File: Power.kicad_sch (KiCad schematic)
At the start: 37 parts, among them J10 Conn_01x01, U4 LMR51625YDDCR, U5 TLV74033PDBVR

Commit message: LCD connector, backlight, other work
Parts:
- removed D10, D12: LED, LED_SMD:LED_0603_1608Metric_Pad1.05x0.95mm_HandSolder, symbol Device:LED
- removed R22: 2.2k, Resistor_SMD:R_0603_1608Metric_Pad0.98x0.95mm_HandSolder, symbol Device:R
- removed R24: 120, Resistor_SMD:R_0603_1608Metric_Pad0.98x0.95mm_HandSolder, symbol Device:R
- D3, D4, D6: footprint Diode_SMD:D_SMA -> Diode_SMD:D_SOD-123F
- L2: value SRU1063A-4R7Y -> 6.8u; footprint Inductor_SMD:L_Bourns-SRU1028_10.0x10.0mm -> Inductor_SMD:L_Bourns-SRN4018

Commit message: fix swd connector orientation, modify 12v input
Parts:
- removed F1: Fuse, Fuse:Fuseholder_Blade_Mini_Keystone_3568, symbol Device:Fuse
- removed J10: Conn_01x01, Connector_PinHeader_2.54mm:PinHeader_1x01_P2.54mm_Vertical, symbol Connector_Generic:Conn_01x01
- removed JP1: SolderJumper_2_Open, Jumper:SolderJumper-2_P1.3mm_Open_RoundedPad1.0x1.5mm, symbol Jumper:SolderJumper_2_Open
- added F1: Polyfuse, Fuse:Fuse_1812_4532Metric_Pad1.30x3.40mm_HandSolder, symbol Device:Polyfuse
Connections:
- net +12V: now also D13.2 (A), F1.2
- net +12V_IN: now also F1.1
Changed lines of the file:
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@@
 	)
 	(junction
-		(at 43.18 82.55)
-		(diameter 0)
-		(color 0 0 0 0)
-	)
-	(junction
 		(at 96.52 110.49)
 		(diameter 0)
@@
 	(wire
 		(pts
-			(xy 35.56 82.55) (xy 43.18 82.55)
-		)
-		(stroke
-			(width 0)
-			(type default)
-		)
-	)
-	(wire
-		(pts
 			(xy 53.34 162.56) (xy 53.34 157.48)
 		)
@@
 	(wire
 		(pts
-			(xy 43.18 82.55) (xy 48.26 82.55)
-		)
-		(stroke
-			(width 0)
-			(type default)
-		)
-	)
-	(wire
-		(pts
 			(xy 73.66 90.17) (xy 80.01 90.17)
 		)
@@
 	(wire
 		(pts
-			(xy 38.1 92.71) (xy 43.18 92.71)
-		)
-		(stroke
-			(width 0)
-			(type default)
-		)
-	)
-	(wire
-		(pts
 			(xy 124.46 80.01) (xy 132.08 80.01)
 		)
@@
 	(wire
 		(pts
-			(xy 43.18 92.71) (xy 43.18 82.55)
-		)
-		(stroke
-			(width 0)
-			(type default)
-		)
-	)
-	(wire
-		(pts
 			(xy 58.42 123.19) (xy 58.42 110.49)
 		)
@@
 	(wire
 		(pts
-			(xy 27.94 82.55) (xy 24.13 82.55)
+			(xy 24.13 82.55) (xy 48.26 82.55)
 		)
 		(stroke
@@
 	)
 	(symbol
-		(lib_id "Jumper:SolderJumper_2_Open")
-		(at 31.75 82.55 0)
-		(unit 1)
-		(exclude_from_sim no)
-		(in_bom no)
-		(on_board yes)
-		(dnp no)
-		(fields_autoplaced yes)
-		(property "Reference" "JP1"
-			(at 31.75 76.2 0)
-			(effects
-				(font
-					(size 1.27 1.27)
-				)
-			)
-		)
-		(property "Value" "SolderJumper_2_Open"
-			(at 31.75 78.74 0)
-			(effects
-				(font
-					(size 1.27 1.27)
-				)
-			)
-		)
-		(property "Footprint" "Jumper:SolderJumper-2_P1.3mm_Open_RoundedPad1.0x1.5mm"
-			(at 31.75 82.55 0)
-			(effects
-				(font
-					(size 1.27 1.27)
-				)
-				(hide yes)
-			)
-		)
-		(property "Datasheet" "~"
-			(at 31.75 82.55 0)
-			(effects
-				(font
-					(size 1.27 1.27)
-				)
-				(hide yes)
-			)
-		)
-		(property "Description" "Solder Jumper, 2-pole, open"
-			(at 31.75 82.55 0)
-			(effects
-				(font
-					(size 1.27 1.27)
-				)
-				(hide yes)
-			)
-		)
-		(pin "2"
-		)
-		(pin "1"
-		)
-		(instances
-			(project ""
-				(path "/f2bb7816-6b2a-47fd-8906-eb4aedd6f9e6/5e700bbe-1f69-4433-b621-e458f2a62014"
-					(reference "JP1")
-					(unit 1)
-				)
-			)
-		)
-	)
-	(symbol
 		(lib_id "Device:R")
 		(at 63.5 38.1 0)
@@
 	)
 	(symbol
+		(lib_id "Device:Polyfuse")
+		(at 50.8 33.02 90)
+		(unit 1)
+		(exclude_from_sim no)
+		(in_bom yes)
+		(on_board yes)
+		(dnp no)
+		(fields_autoplaced yes)
+		(property "Reference" "F1"
+			(at 50.8 26.67 90)
+			(effects
+				(font
+					(size 1.27 1.27)
+				)
+			)
+		)
+		(property "Value" "Polyfuse"
+			(at 50.8 29.21 90)
+			(effects
+				(font
+					(size 1.27 1.27)
+				)
+			)
+		)
+		(property "Footprint" "Fuse:Fuse_1812_4532Metric_Pad1.30x3.40mm_HandSolder"
+			(at 55.88 31.75 0)
+			(effects
+				(font
+					(size 1.27 1.27)
+				)
+				(justify left)
+				(hide yes)
+			)
+		)
+		(property "Datasheet" "~"
+			(at 50.8 33.02 0)
+			(effects
+				(font
+					(size 1.27 1.27)
+				)
+				(hide yes)
+			)
+		)
+		(property "Description" "Resettable fuse, polymeric positive temperature coefficient"
+			(at 50.8 33.02 0)
+			(effects
+				(font
+					(size 1.27 1.27)
+				)
+				(hide yes)
+			)
+		)
+		(pin "2"
+		)
+		(pin "1"
+		)
+		(instances
+			(project "LV3-Dash"
+				(path "/f2bb7816-6b2a-47fd-8906-eb4aedd6f9e6/5e700bbe-1f69-4433-b621-e458f2a62014"
+					(reference "F1")
+					(unit 1)
+				)
+			)
+		)
+	)
+	(symbol
 		(lib_id "Device:C")
 		(at 43.18 161.29 0)
@@
 	)
 	(symbol
-		(lib_id "Device:Fuse")
-		(at 50.8 33.02 90)
-		(unit 1)
-		(exclude_from_sim no)
-		(in_bom yes)
-		(on_board yes)
-		(dnp no)
-		(fields_autoplaced yes)
-		(property "Reference" "F1"
-			(at 50.8 26.67 90)
-			(effects
-				(font
-					(size 1.27 1.27)
-				)
-			)
-		)
-		(property "Value" "Fuse"
-			(at 50.8 29.21 90)
-			(effects
-				(font
-					(size 1.27 1.27)
-				)
-			)
-		)
-		(property "Footprint" "Fuse:Fuseholder_Blade_Mini_Keystone_3568"
-			(at 50.8 34.798 90)
-			(effects
-				(font
-					(size 1.27 1.27)
-				)
-				(hide yes)
-			)
-		)
-		(property "Datasheet" "~"
-			(at 50.8 33.02 0)
-			(effects
-				(font
-					(size 1.27 1.27)
-				)
-				(hide yes)
-			)
-		)
-		(property "Description" "Fuse"
-			(at 50.8 33.02 0)
-			(effects
-				(font
-					(size 1.27 1.27)
-				)
-				(hide yes)
-			)
-		)
-		(pin "2"
-		)
-		(pin "1"
-		)
-		(instances
-			(project ""
-				(path "/f2bb7816-6b2a-47fd-8906-eb4aedd6f9e6/5e700bbe-1f69-4433-b621-e458f2a62014"
-					(reference "F1")
-					(unit 1)
-				)
-			)
-		)
-	)
-	(symbol
 		(lib_id "Device:C")
 		(at 76.2 46.99 0)
@@
 					(unit 1)
 				)
-			)
-		)
-	)
-	(symbol
-		(lib_id "Connector_Generic:Conn_01x01")
-		(at 33.02 92.71 180)
-		(unit 1)
-		(exclude_from_sim no)
-		(in_bom yes)
-		(on_board yes)
-		(dnp no)
-		(fields_autoplaced yes)
-		(property "Reference" "J10"
-			(at 33.02 86.36 0)
-			(effects
-				(font
-					(size 1.27 1.27)
-				)
-			)
-		)
-		(property "Value" "Conn_01x01"
-			(at 33.02 88.9 0)
-			(effects
-				(font
-					(size 1.27 1.27)
-				)
-			)
-		)
-		(property "Footprint" "Connector_PinHeader_2.54mm:PinHeader_1x01_P2.54mm_Vertical"
-			(at 33.02 92.71 0)
-			(effects
-				(font
-					(size 1.27 1.27)
-				)
-				(hide yes)
-			)
-		)
-		(property "Datasheet" "~"
-			(at 33.02 92.71 0)
-			(effects
-				(font
-					(size 1.27 1.27)
-				)
-				(hide yes)
-			)
-		)
-		(property "Description" "Generic connector, single row, 01x01, script generated (kicad-library-utils/schlib/autogen/connector/)"
-			(at 33.02 92.71 0)
-			(effects
-				(font
-					(size 1.27 1.27)
-				)
-				(hide yes)
-			)
-		)
-		(pin "1"
-		)
-		(instances
-			(project "LV3-Core"
-				(path "/f2bb7816-6b2a-47fd-8906-eb4aedd6f9e6/5e700bbe-1f69-4433-b621-e458f2a62014"
-					(reference "J10")
-					(unit 1)
-				)

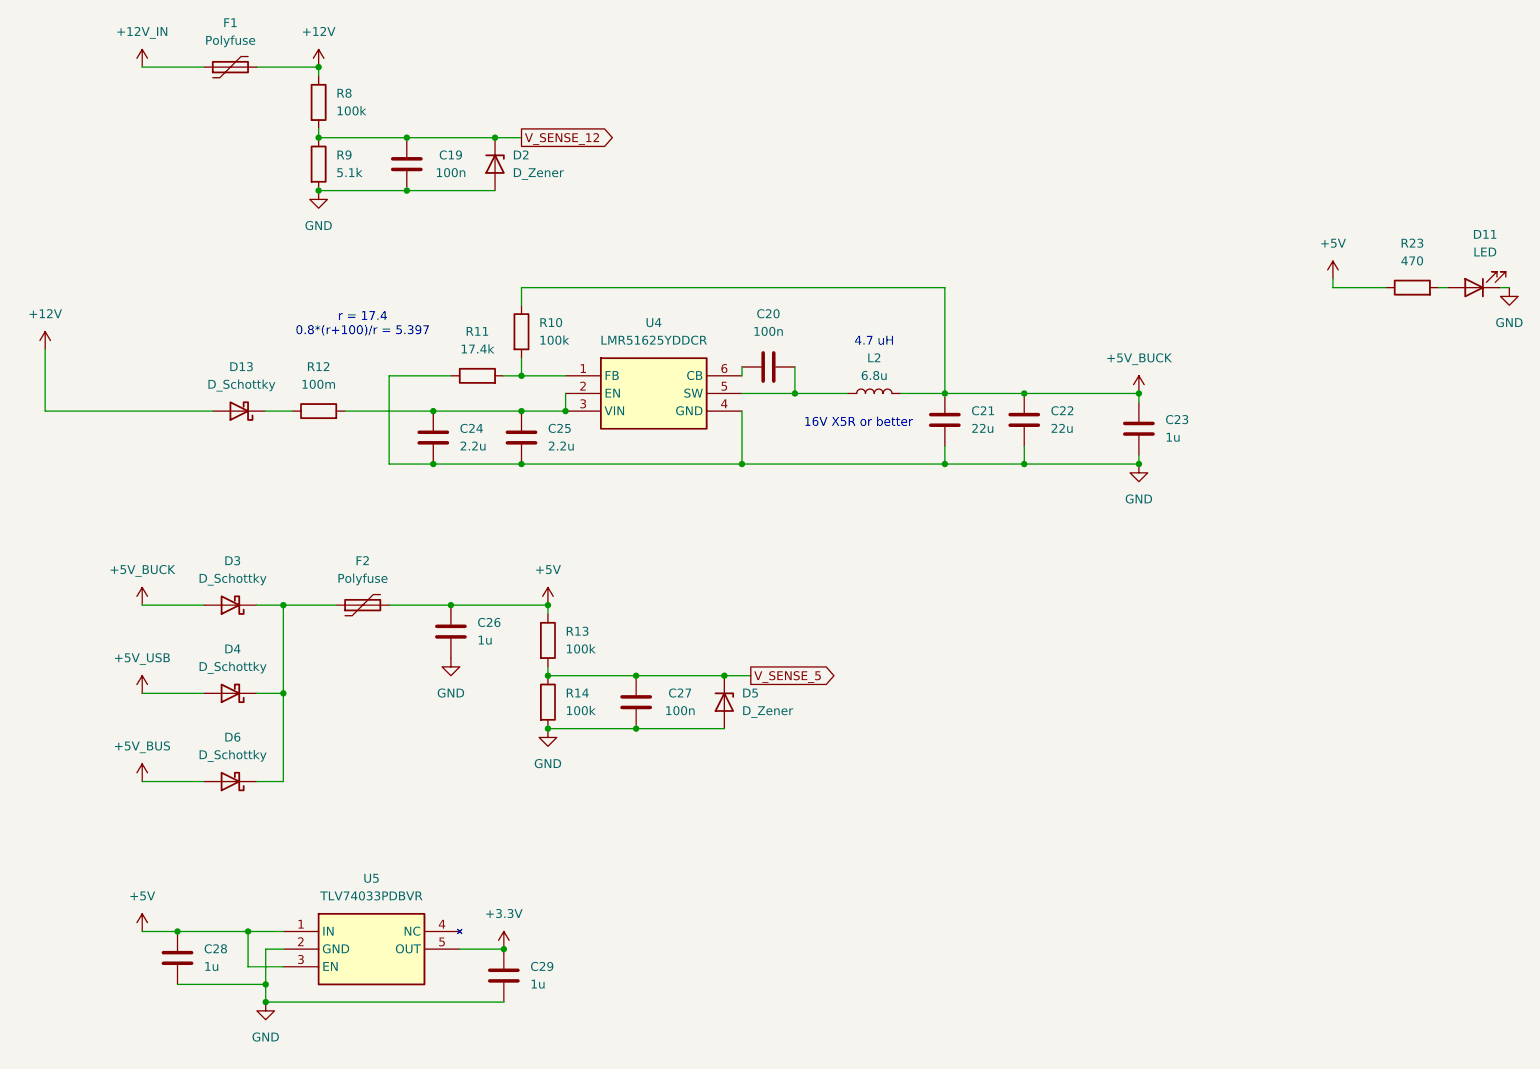
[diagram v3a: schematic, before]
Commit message: basic layout organization, fix +VDDA typo
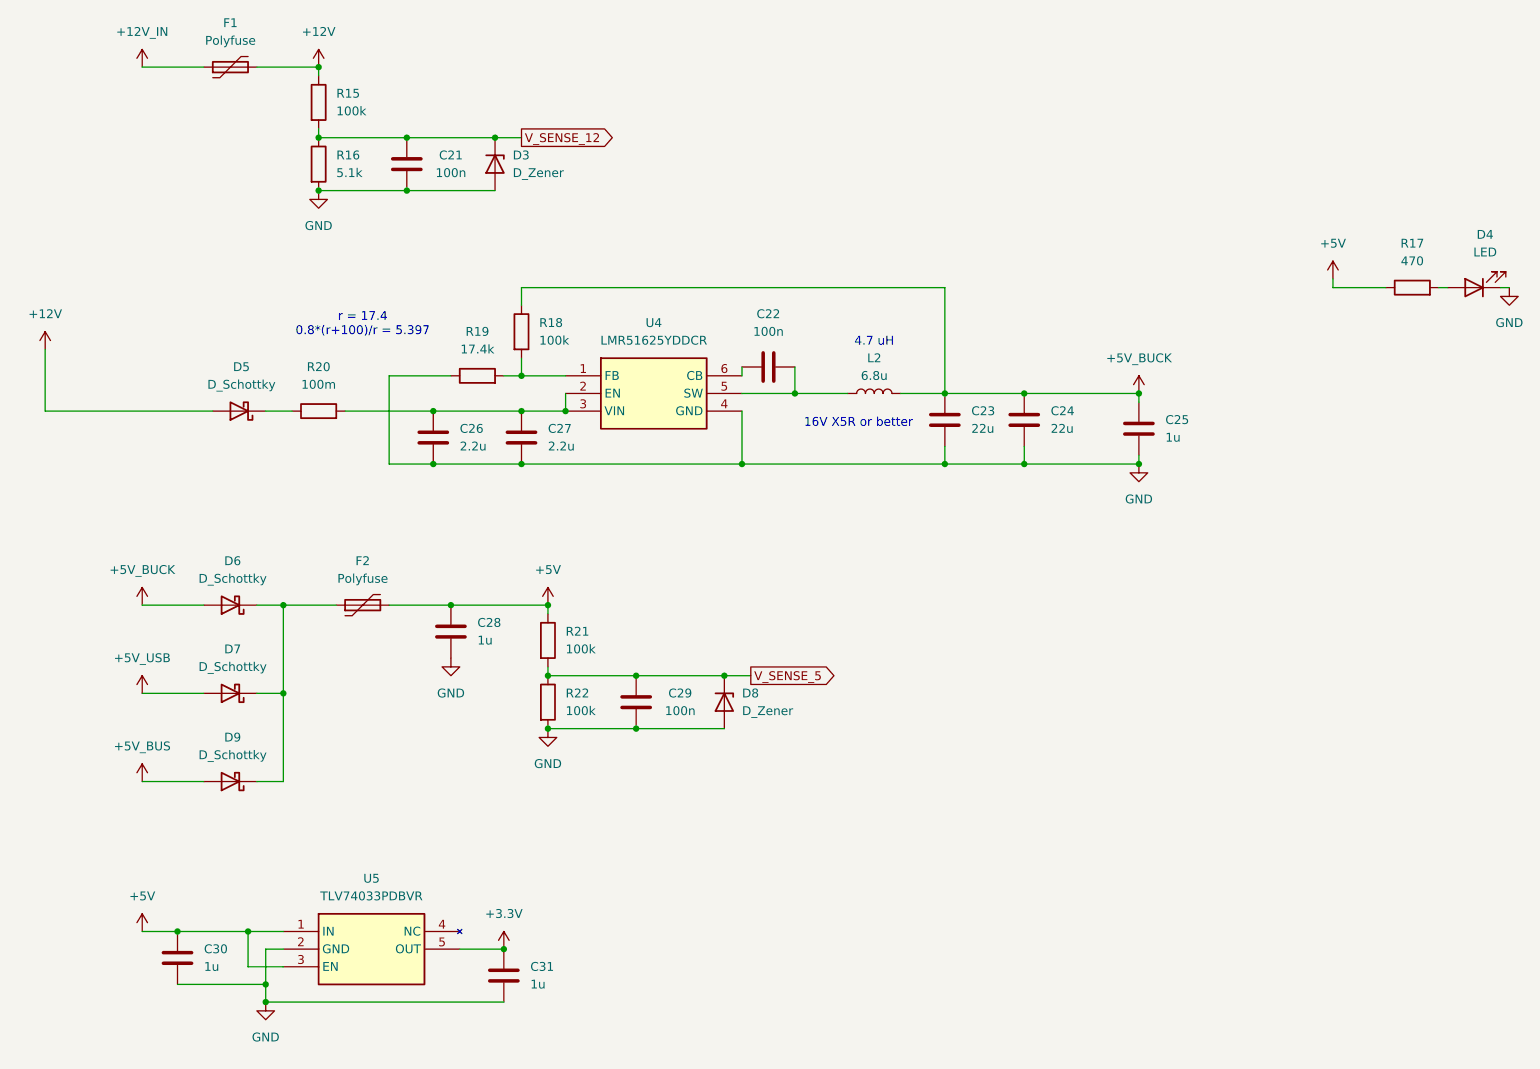
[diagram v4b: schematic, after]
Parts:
- renumbered C19 to C21, C20 to C22, C21 to C23, C22 to C24, C23 to C25, C24 to C26, C25 to C27, C26 to C28, C27 to C29, C28 to C30, C29 to C31, D2 to D3, D11 to D4, D13 to D5, D3 to D6, D4 to D7, D5 to D8, D6 to D9, R8 to R15, R9 to R16, R23 to R17, R10 to R18, R11 to R19, R12 to R20, R13 to R21, R14 to R22

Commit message: 3.3v regulator changes, GPIO output fixes, layout changes
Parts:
- removed C28: 1u, Capacitor_SMD:C_0603_1608Metric_Pad1.08x0.95mm_HandSolder, symbol Device:C
- removed U5: TLV74033PDBVR, SamacSys_Parts:SOT95P280X145-5N, symbol SamacSys_Parts:TLV74033PDBVR
- added U7: AMS1117-3.3, Package_TO_SOT_SMD:SOT-223-3_TabPin2, symbol Regulator_Linear:AMS1117-3.3
- C31: value 1u -> 22u; footprint Capacitor_SMD:C_0603_1608Metric_Pad1.08x0.95mm_HandSolder -> Capacitor_SMD:C_1206_3216Metric_Pad1.33x1.80mm_HandSolder
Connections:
- net +3.3V: now also U7.2 (VO)
- net +5V: now also U7.3 (VI)
- net GND: now also U7.1 (GND)
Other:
- moved on the sheet: C30
